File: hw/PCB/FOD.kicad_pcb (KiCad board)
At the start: 2 copper layers, 47.8 x 95.5 mm, 34 parts, among them J1 USB_B_Micro, J2 U.FL, J3 Nichrome, J4 Programmer, Q1 PMV16XNR, SW1 Reset_push, U0 Payload, U1 SAMD21E, U2 AP7215-33YG-13, U3 RFM69HCW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

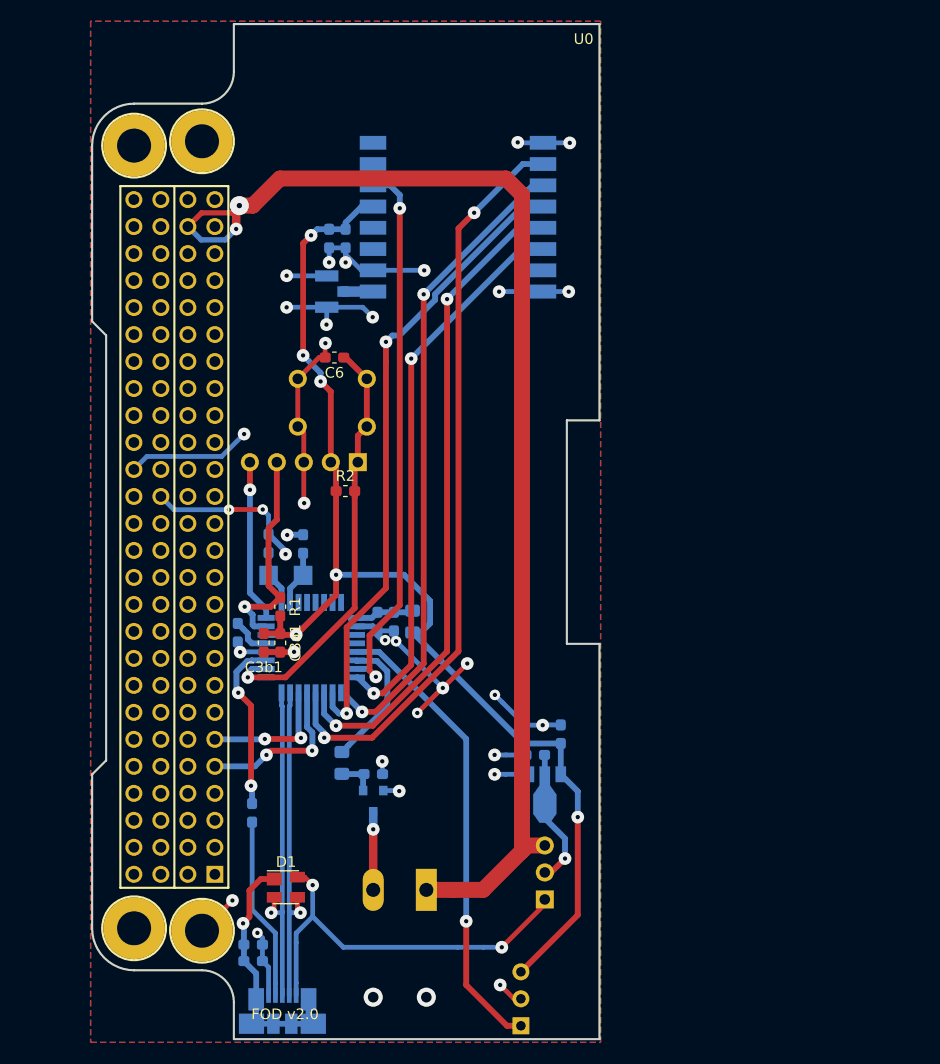
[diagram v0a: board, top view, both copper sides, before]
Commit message: Created a new PCB for the Femto-satellite Orbital Deployer (FOD). Instead of using the PC104 standard, it now has the shape of a type A interstage panel. Added a data logger. Deleted old files from the previews version.
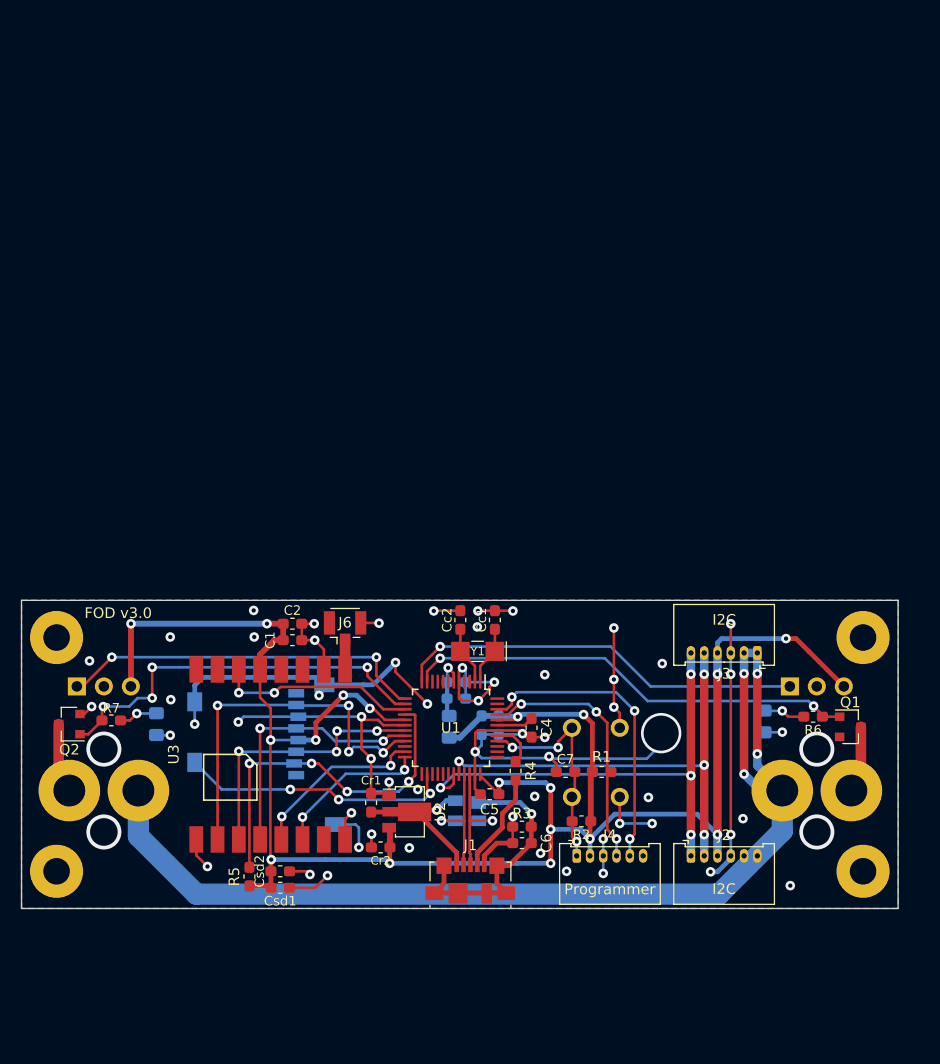
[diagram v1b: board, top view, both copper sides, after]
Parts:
- removed JP1: Jumper, Connector_PinHeader_2.54mm:PinHeader_1x03_P2.54mm_Vertical
- removed U0: Payload, Payload:FOD
- added C7: 100nF, Capacitor_SMD:C_0603_1608Metric_Pad1.05x0.95mm_HandSolder, F.Cu at (151.2, 96.2)
- added Csd1: 10uF, Capacitor_SMD:C_0603_1608Metric_Pad1.05x0.95mm_HandSolder, F.Cu at (124.3, 107.0)
- added Csd2: 100nF, Capacitor_SMD:C_0603_1608Metric_Pad1.05x0.95mm_HandSolder, F.Cu at (124.3, 105.5)
- added D3: LED, Diode_SMD:D_0805_2012Metric_Pad1.15x1.40mm_HandSolder, B.Cu at (112.7, 91.7)
- added J5: Micro_SD_Card_Det, SD:microSD_socket, B.Cu at (117.0, 92.6)
- added J6: U.FL, Connector_Coaxial:U.FL_Hirose_U.FL-R-SMT-1_Vertical, F.Cu at (130.4, 82.6)
- added Q2: PMV16XNR, Package_TO_SOT_SMD:SOT-23, F.Cu at (104.5, 91.7)
- added R6: 330, Resistor_SMD:R_0603_1608Metric_Pad1.05x0.95mm_HandSolder, F.Cu at (174.5, 91.0)
- added R7: 330, Resistor_SMD:R_0603_1608Metric_Pad1.05x0.95mm_HandSolder, F.Cu at (108.5, 91.3)
- added U5: AV4524, Interrupt:AV4524, B.Cu at (107.8, 88.1)
- added U6: DPL, Interstage:Type-A, F.Cu at (100.0, 80.0)
- C1, C2, C4, Cc1, Cc2, Cr1, Cr2, J1, Q1, R3, R4, U2, U3, Y1: moved to F.Cu
- C3a1, C3b1, D1: moved to B.Cu
- C5: value 4.7nF -> 100nF; moved to F.Cu
- C6: value 100nF -> 4.7nF
- J2: value U.FL -> I2C; footprint Connector_Coaxial:U.FL_Hirose_U.FL-R-SMT-1_Vertical -> Connector_Molex:Molex_PicoBlade_53048-0610_1x06_P1.25mm_Horizontal; moved to F.Cu
- J3: value Nichrome -> I2C; footprint TerminalBlock:TerminalBlock_Altech_AK300-2_P5.00mm -> Connector_Molex:Molex_PicoBlade_53048-0610_1x06_P1.25mm_Horizontal; moved to F.Cu
- J4: footprint Connector_PinHeader_2.54mm:PinHeader_1x05_P2.54mm_Vertical -> Connector_Molex:Molex_PicoBlade_53048-0610_1x06_P1.25mm_Horizontal; moved to F.Cu
- R5: value 330 -> 100k; moved to F.Cu
- U1: value SAMD21E -> SAMD21G; footprint Package_QFP:TQFP-32_7x7mm_P0.8mm -> Package_QFP:TQFP-48_7x7mm_P0.5mm; moved to F.Cu
- moved J2 63.0 mm to (163.0, 104.0), turned to 0 degrees
- moved U3 53.5 mm to (123.5, 94.5), turned to 90 degrees
- moved C6 49.0 mm to (147.1, 102.8)
- moved Q1 45.4 mm to (178.0, 91.9), turned to 0 degrees
- moved J4 42.4 mm to (152.2, 104.0), turned to 0 degrees
- moved U4 40.5 mm to (174.8, 88.1), turned to -90 degrees
- moved D2 39.9 mm to (169.9, 91.4)
- moved SW1 38.3 mm to (151.8, 92.0), turned to -90 degrees
- moved J3 38.3 mm to (169.2, 85.0)
- moved R2 38.2 mm to (152.7, 100.8), turned to 180 degrees
- moved C1 38.0 mm to (125.5, 83.8), turned to 0 degrees
- moved C2 36.6 mm to (125.5, 82.2), turned to 0 degrees
- moved R1 34.0 mm to (154.6, 96.2), turned to 0 degrees
- moved C4 29.1 mm to (148.0, 92.0)
- moved R3 27.6 mm to (147.1, 101.3), turned to 180 degrees
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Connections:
- C5 pad 1: /USB/SHIELD -> +3V3
- C6 pad 1: /RESET -> /USB/SHIELD
- Cr1 pad 1: /Power/5V0 -> /VUSB
- D2 pad 1: Net-(D2-Pad1) -> GND
- D2 pad 2: /DPL_EN -> Net-(D2-Pad2)
- J2 pad 1: /Communication/ANT -> /SDA
- J2 pad 2: GND -> /SCL
- J3 pad 2: Net-(J3-Pad2) -> /VIN
- Q1 pad 1: Net-(D2-Pad1) -> /DPL_EN1
- Q1 pad 3: Net-(J3-Pad2) -> /Deploy/PORT1
- R5 pad 1: Net-(D2-Pad1) -> +3V3
- R5 pad 2: GND -> /DL_NSS
- SW1 pad 1: GND -> /RESET
- SW1 pad 4: /RESET -> GND
- U1 pad 10: GND -> Net-(U1-Pad10)
- U1 pad 11: Net-(U1-Pad11) -> /DPL_EN1
- U1 pad 12: Net-(U1-Pad12) -> /DPL_STA1
- U1 pad 13: /DPL_STA -> /DPL_STA2
- U1 pad 14: /DPL_EN -> /DPL_EN2
- U1 pad 16: /TRX_RST -> /DL_NSS
- U1 pad 17: /MOSI -> +3V3
- U1 pad 18: /SCK -> GND
- U1 pad 19: /TRX_NSS -> /MOSI
- U1 pad 20: /MISO -> /SCK
- U1 pad 21: /SDA -> /MISO
- U1 pad 22: /SCL -> Net-(U1-Pad22)
- U1 pad 23: /USB_N -> /TRX_NSS
- U1 pad 24: /USB_P -> /TRX_RST
- U1 pad 26: /RESET -> /DL_CD
- U1 pad 27: /USB_ID -> Net-(U1-Pad27)
- U1 pad 28: GND -> Net-(U1-Pad28)
- U1 pad 29: /VDDCORE -> Net-(U1-Pad29)
- U1 pad 30: +3V3 -> Net-(U1-Pad30)
- U1 pad 31: /SWCLK -> /SDA
- U1 pad 32: /SWDIO -> /SCL
- U1 pad 5: Net-(U1-Pad5) -> GND
- U1 pad 6: Net-(U1-Pad6) -> /VDDANA
- U1 pad 9: /VDDANA -> Net-(U1-Pad9)
- U2 pad 2: /Power/5V0 -> /VUSB
- U4 pad 1: /DPL_STA -> /DPL_STA1
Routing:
- net +3V3: track 112.3 -> 192.6 mm, vias 6 -> 18
- net GND: track 137.7 -> 197.1 mm, vias 34 -> 63
- net /TRX_NSS: track 61.9 -> 16.8 mm
- net /DPL_STA: track 43.6 -> 0.00 mm, vias 1 -> 0
- net /DPL_EN1: track 0.00 -> 42.7 mm, vias 0 -> 2
- net /DPL_STA1: track 0.00 -> 38.5 mm, vias 0 -> 1
- net /TRX_RST: track 52.4 -> 14.8 mm
- net /DPL_EN2: track 0.00 -> 37.5 mm, vias 0 -> 4
- net /MISO: track 70.8 -> 35.5 mm, vias 2 -> 4
- net /SCK: track 59.8 -> 24.8 mm
- net /MOSI: track 60.6 -> 25.9 mm, vias 2 -> 4
- net /DPL_STA2: track 0.00 -> 34.6 mm, vias 0 -> 2
- net /DL_NSS: track 0.00 -> 33.7 mm, vias 0 -> 4
- net /TRX_INT: track 51.8 -> 18.9 mm
- net /SCL: track 12.5 -> 43.6 mm, vias 2 -> 4
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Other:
- board size 47.8 x 95.5 mm -> 82.5 x 29 mm
- net class ANT removed
- net class Default: trace_width 0.55 -> 0.25; via_dia 1.2 -> 0.9
- net class Picoblade added: clearance 0.2, trace_width 0.8, via_dia 0.9, via_drill 0.4
- net class Power: trace_width 1.5 -> 2; via_dia 1.2 -> 2; via_drill 0.4 -> 0.6
- net class Power2 added: clearance 0.2, trace_width 0.55, via_dia 0.9, via_drill 0.4
- net class Stack removed
- net class USB: via_dia 1.2 -> 0.9
- net class uC removed
- rule pad_to_mask_clearance: 0.051 -> 0.05
- board text added: "FOD v3.0"
- board text removed: "3V3"
- board text removed: "5V0"
- board text removed: "DPLY"
- board text removed: "FOD v2.0"
- board text removed: "GND"
- board text removed: "RST"
- board text removed: "SWC"
- board text removed: "SWD"
- board text removed: "VIN"
- board text removed: "VUSB"

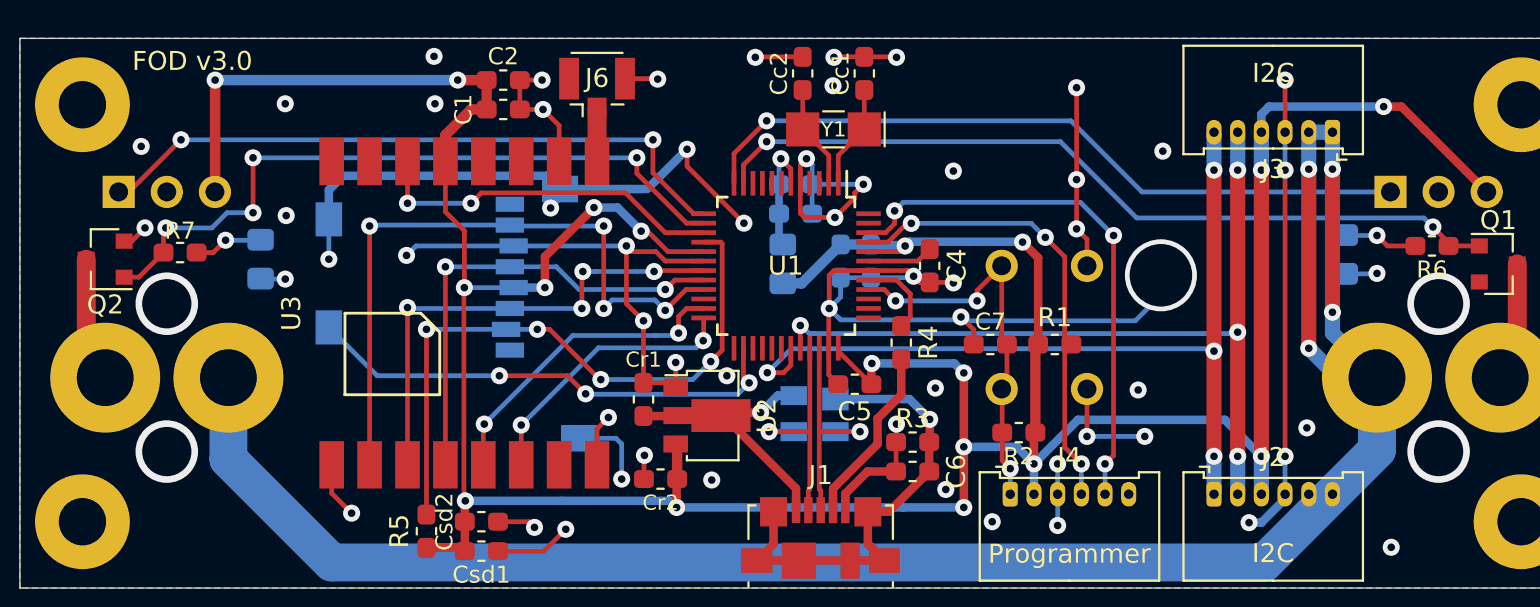
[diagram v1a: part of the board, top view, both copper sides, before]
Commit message: Improved the trace routing to increase the ground plane. Added text labels for some connectors.
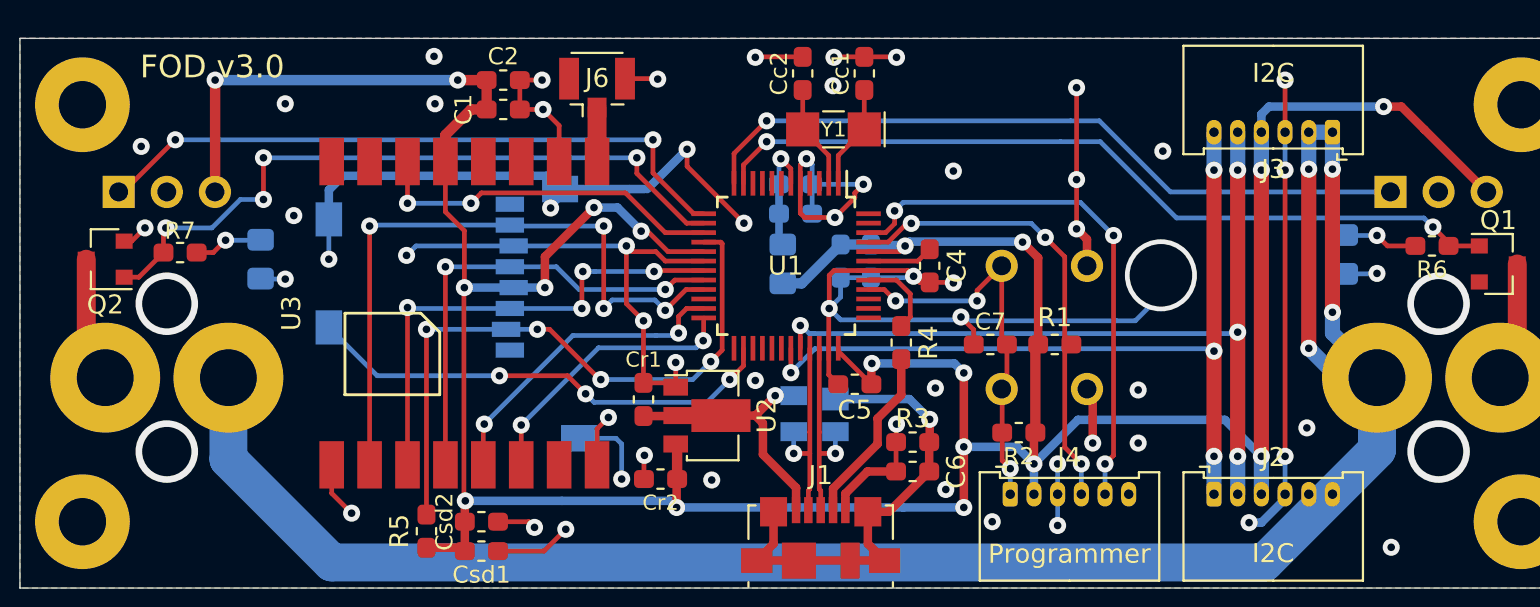
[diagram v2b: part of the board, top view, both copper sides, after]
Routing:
- net /VUSB: track 17.4 -> 14.5 mm
- net GND: track 197.1 -> 194.6 mm
- net /SDA: track 45.5 -> 43.3 mm
- net /USB_P: track 12.0 -> 10.6 mm
- net /USB_N: track 12.0 -> 10.6 mm
- net /DL_CD: track 25.8 -> 25.3 mm
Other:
- board text added: "3V3"
- board text added: "GND"
- board text added: "PORT1"
- board text added: "PORT2"
- board text added: "RESET"
- board text added: "RST"
- board text added: "SCL"
- board text added: "SDA"
- board text added: "SWC"
- board text added: "SWD"
- board text added: "VIN"

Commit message: Separated the VIN power line into two independent power lines (VAUX and VAUX2). This is done to add compatibility with other CubeSats standards. Added the option to bridge those lines with a zero Ohm resistor.
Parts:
- added R8: 0, Resistor_SMD:R_0603_1608Metric_Pad1.05x0.95mm_HandSolder, F.Cu at (168.9, 101.7)
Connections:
- J2 pad 5: /VIN -> /VAUX2
- J2 pad 6: /VIN -> /VAUX
- J3 pad 1: /VIN -> /VAUX
- J3 pad 2: /VIN -> /VAUX2
- U6 pad 1: /VIN -> /VAUX
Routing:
- net /VIN: track 106.4 -> 0.00 mm, vias 4 -> 0
- net /VAUX: track 0.00 -> 99.3 mm, vias 0 -> 3
- net /VAUX2: track 0.00 -> 19.1 mm, vias 0 -> 2
- net GND: track 194.6 -> 192.2 mm
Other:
- board text added: "VAUX"
- board text added: "VAUX2"
- board text removed: "VIN"
